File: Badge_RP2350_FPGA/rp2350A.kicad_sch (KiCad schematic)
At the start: 33 parts, among them J2 Conn_01x03_Pin, SW1 SW_Push, SW2 SW_Push, U1 RP2350_60QFN, U7 W25Q32JVSS, Y1 ABM8-272-T3

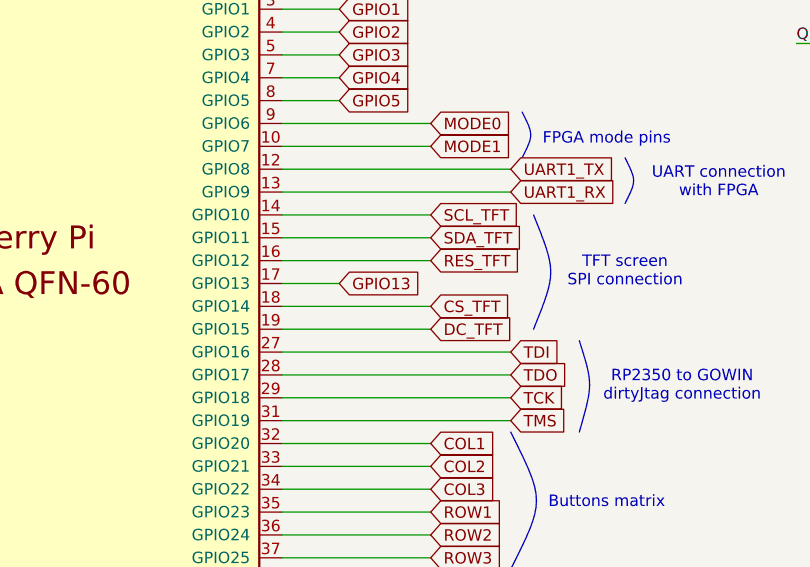
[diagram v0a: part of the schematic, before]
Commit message: add jtagsel_n connection
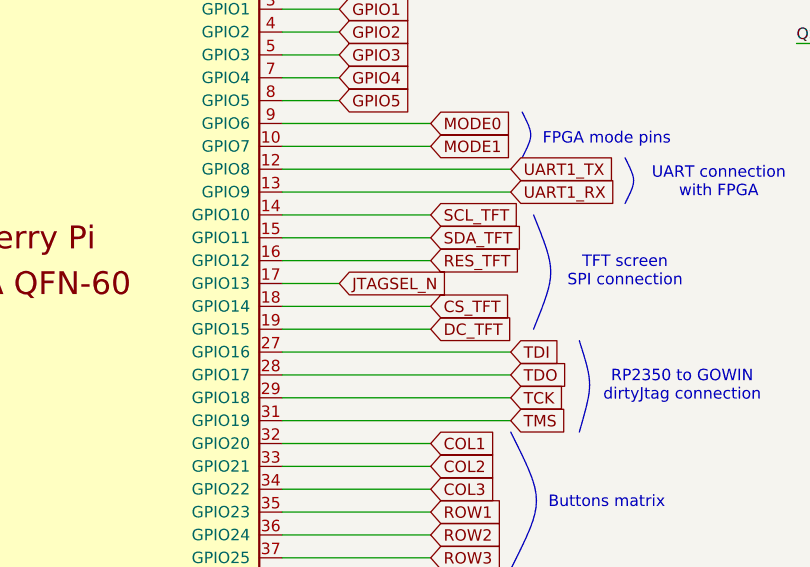
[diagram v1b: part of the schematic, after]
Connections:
- net GPIO13 renamed JTAGSEL_N
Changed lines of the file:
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@@
 		(title "RISC-V Summit Europe Badge")
 		(date "2026-03-29")
-		(rev "v1.4")
+		(rev "v1.42")
 		(company "SemiTO-V, RISC-V Student Team")
 		(comment 3 "License: CERN-OHL-W-2.0")
@@
 		)
 	)
-	(global_label "GPIO13"
-		(shape input)
-		(at 151.13 106.68 0)
-		(fields_autoplaced yes)
-		(effects
-			(font
-				(size 1.27 1.27)
-			)
-			(justify left)
-		)
-		(property "Intersheetrefs" "${INTERSHEET_REFS}"
-			(at 161.0095 106.68 0)
-			(hide yes)
-			(show_name no)
-			(do_not_autoplace no)
-			(effects
-				(font
-					(size 1.27 1.27)
-				)
-				(justify left)
-			)
-		)
-	)
 	(global_label "UART1_RX"
 		(shape input)
@@
 			(hide yes)
 			(show_name no)
+			(do_not_autoplace no)
+			(effects
+				(font
+					(size 1.27 1.27)
+				)
+				(justify left)
+			)
+		)
+	)
+	(global_label "JTAGSEL_N"
+		(shape input)
+		(at 151.13 106.68 0)
+		(fields_autoplaced yes)
+		(effects
+			(font
+				(size 1.27 1.27)
+			)
+			(justify left)
+		)
+		(property "Intersheetrefs" "${INTERSHEET_REFS}"
+			(at 164.0937 106.68 0)
+			(hide yes)
+			(show_name no)

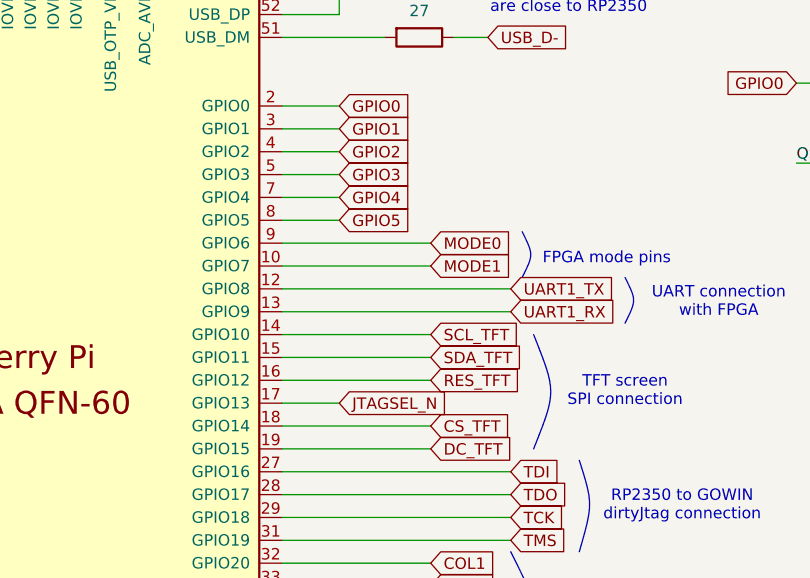
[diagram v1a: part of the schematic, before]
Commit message: add more FPGA connections and generate netlist, bom
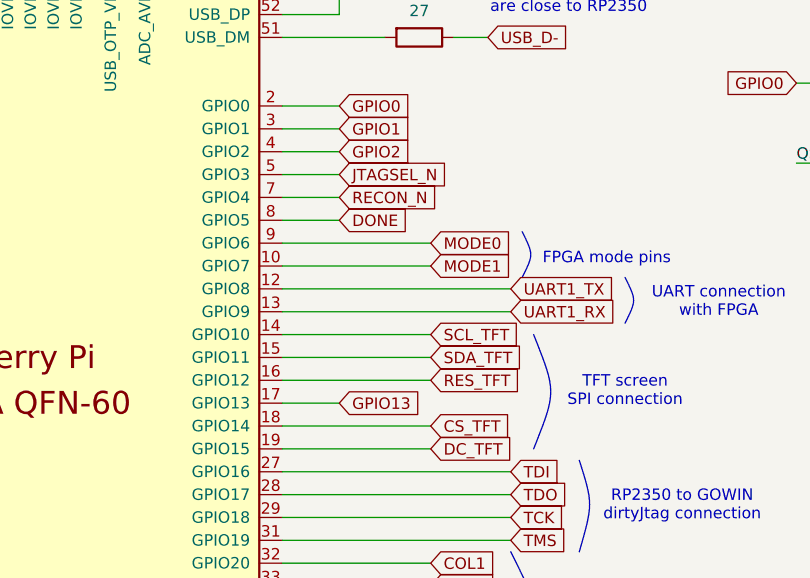
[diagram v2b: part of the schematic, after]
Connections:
- net GPIO3 is gone; now on net JTAGSEL_N: U1.5 (GPIO3)
- net JTAGSEL_N: no longer U1.17 (GPIO13)
- net GPIO4 renamed RECON_N
- net GPIO5 renamed DONE
- new net GPIO13: U1.17 (GPIO13)
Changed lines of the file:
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@@
 		)
 	)
-	(global_label "GPIO3"
+	(global_label "UART1_RX"
+		(shape input)
+		(at 170.18 96.52 0)
+		(fields_autoplaced yes)
+		(effects
+			(font
+				(size 1.27 1.27)
+			)
+			(justify left)
+		)
+		(property "Intersheetrefs" "${INTERSHEET_REFS}"
+			(at 182.4785 96.52 0)
+			(hide yes)
+			(show_name no)
+			(do_not_autoplace no)
+			(effects
+				(font
+					(size 1.27 1.27)
+				)
+				(justify left)
+			)
+		)
+	)
+	(global_label "GPIO28_ADC2"
+		(shape input)
+		(at 151.13 147.32 0)
+		(fields_autoplaced yes)
+		(effects
+			(font
+				(size 1.27 1.27)
+			)
+			(justify left)
+		)
+		(property "Intersheetrefs" "${INTERSHEET_REFS}"
+			(at 166.8152 147.32 0)
+			(hide yes)
+			(show_name no)
+			(do_not_autoplace no)
+			(effects
+				(font
+					(size 1.27 1.27)
+				)
+				(justify left)
+			)
+		)
+	)
+	(global_label "GPIO27_ADC1"
+		(shape input)
+		(at 151.13 144.78 0)
+		(fields_autoplaced yes)
+		(effects
+			(font
+				(size 1.27 1.27)
+			)
+			(justify left)
+		)
+		(property "Intersheetrefs" "${INTERSHEET_REFS}"
+			(at 166.8152 144.78 0)
+			(hide yes)
+			(show_name no)
+			(do_not_autoplace no)
+			(effects
+				(font
+					(size 1.27 1.27)
+				)
+				(justify left)
+			)
+		)
+	)
+	(global_label "JTAGSEL_N"
 		(shape input)
 		(at 151.13 81.28 0)
@@
 		)
 		(property "Intersheetrefs" "${INTERSHEET_REFS}"
-			(at 159.8 81.28 0)
-			(hide yes)
-			(show_name no)
-			(do_not_autoplace no)
-			(effects
-				(font
-					(size 1.27 1.27)
-				)
-				(justify left)
-			)
-		)
-	)
-	(global_label "UART1_RX"
-		(shape input)
-		(at 170.18 96.52 0)
-		(fields_autoplaced yes)
-		(effects
-			(font
-				(size 1.27 1.27)
-			)
-			(justify left)
-		)
-		(property "Intersheetrefs" "${INTERSHEET_REFS}"
-			(at 182.4785 96.52 0)
-			(hide yes)
-			(show_name no)
-			(do_not_autoplace no)
-			(effects
-				(font
-					(size 1.27 1.27)
-				)
-				(justify left)
-			)
-		)
-	)
-	(global_label "GPIO28_ADC2"
-		(shape input)
-		(at 151.13 147.32 0)
-		(fields_autoplaced yes)
-		(effects
-			(font
-				(size 1.27 1.27)
-			)
-			(justify left)
-		)
-		(property "Intersheetrefs" "${INTERSHEET_REFS}"
-			(at 166.8152 147.32 0)
-			(hide yes)
-			(show_name no)
-			(do_not_autoplace no)
-			(effects
-				(font
-					(size 1.27 1.27)
-				)
-				(justify left)
-			)
-		)
-	)
-	(global_label "GPIO27_ADC1"
-		(shape input)
-		(at 151.13 144.78 0)
-		(fields_autoplaced yes)
-		(effects
-			(font
-				(size 1.27 1.27)
-			)
-			(justify left)
-		)
-		(property "Intersheetrefs" "${INTERSHEET_REFS}"
-			(at 166.8152 144.78 0)
+			(at 164.0937 81.28 0)
 			(hide yes)
 			(show_name no)
@@
 		)
 	)
+	(global_label "DONE"
+		(shape input)
+		(at 151.13 86.36 0)
+		(fields_autoplaced yes)
+		(effects
+			(font
+				(size 1.27 1.27)
+			)
+			(justify left)
+		)
+		(property "Intersheetrefs" "${INTERSHEET_REFS}"
+			(at 159.1952 86.36 0)
+			(hide yes)
+			(show_name no)
+			(do_not_autoplace no)
+			(effects
+				(font
+					(size 1.27 1.27)
+				)
+				(justify left)
+			)
+		)
+	)
 	(global_label "SDA_TFT"
 		(shape input)
@@
 		)
 	)
+	(global_label "RECON_N"
+		(shape input)
+		(at 151.13 83.82 0)
+		(fields_autoplaced yes)
+		(effects
+			(font
+				(size 1.27 1.27)
+			)
+			(justify left)
+		)
+		(property "Intersheetrefs" "${INTERSHEET_REFS}"
+			(at 162.7633 83.82 0)
+			(hide yes)
+			(show_name no)
+			(do_not_autoplace no)
+			(effects
+				(font
+					(size 1.27 1.27)
+				)
+				(justify left)
+			)
+		)
+	)
+	(global_label "GPIO13"
+		(shape input)
+		(at 151.13 106.68 0)
+		(fields_autoplaced yes)
+		(effects
+			(font
+				(size 1.27 1.27)
+			)
+			(justify left)
+		)
+		(property "Intersheetrefs" "${INTERSHEET_REFS}"
+			(at 161.0095 106.68 0)
+			(hide yes)
+			(show_name no)
+			(do_not_autoplace no)
+			(effects
+				(font
+					(size 1.27 1.27)
+				)
+				(justify left)
+			)
+		)
+	)
 	(global_label "GPIO29_ADC3"
 		(shape input)
@@
 		)
 	)
-	(global_label "GPIO5"
-		(shape input)
-		(at 151.13 86.36 0)
-		(fields_autoplaced yes)
-		(effects
-			(font
-				(size 1.27 1.27)
-			)
-			(justify left)
-		)
-		(property "Intersheetrefs" "${INTERSHEET_REFS}"
-			(at 159.8 86.36 0)
-			(hide yes)
-			(show_name no)
-			(do_not_autoplace no)
-			(effects
-				(font
-					(size 1.27 1.27)
-				)
-				(justify left)
-			)
-		)
-	)
-	(global_label "JTAGSEL_N"
-		(shape input)
-		(at 151.13 106.68 0)
-		(fields_autoplaced yes)
-		(effects
-			(font
-				(size 1.27 1.27)
-			)
-			(justify left)
-		)
-		(property "Intersheetrefs" "${INTERSHEET_REFS}"
-			(at 164.0937 106.68 0)
-			(hide yes)
-			(show_name no)
-			(do_not_autoplace no)
-			(effects
-				(font
-					(size 1.27 1.27)
-				)
-				(justify left)
-			)
-		)
-	)
 	(global_label "COL2"
 		(shape input)
@@
 			(hide yes)
 			(show_name no)
-			(do_not_autoplace no)
-			(effects
-				(font
-					(size 1.27 1.27)
-				)
-				(justify left)
-			)
-		)
-	)
-	(global_label "GPIO4"
-		(shape input)
-		(at 151.13 83.82 0)
-		(fields_autoplaced yes)
-		(effects
-			(font
-				(size 1.27 1.27)
-			)
-			(justify left)
-		)
-		(property "Intersheetrefs" "${INTERSHEET_REFS}"
-			(at 159.8 83.82 0)
-			(hide yes)
-			(show_name no)

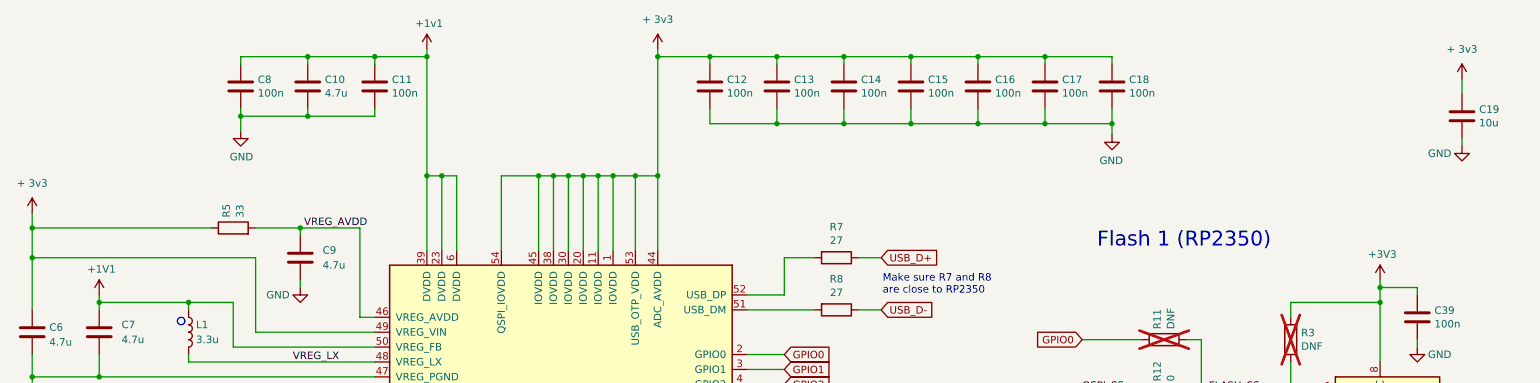
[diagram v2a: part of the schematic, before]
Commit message: update footprints, connections, some labels and more
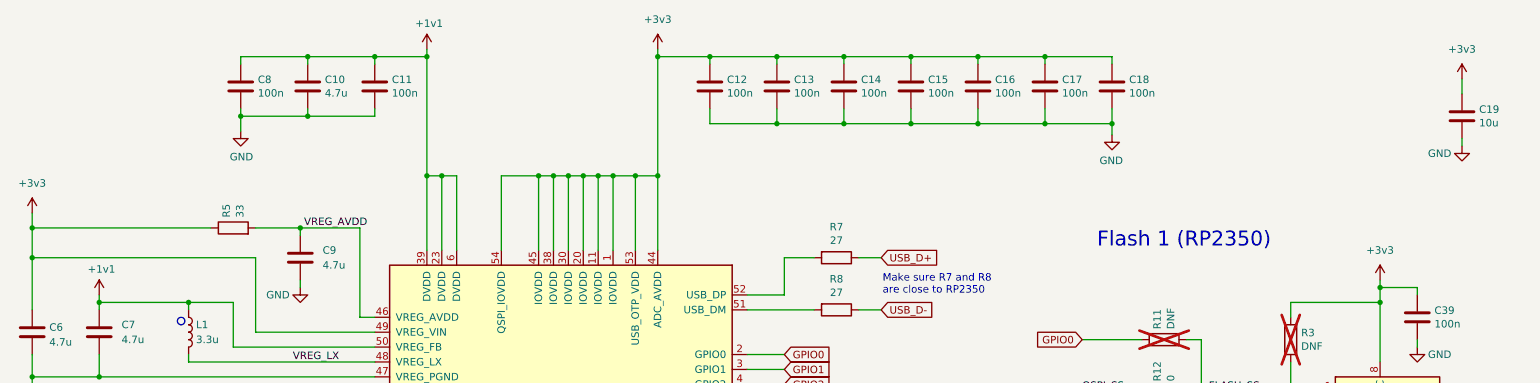
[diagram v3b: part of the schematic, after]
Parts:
- SW1, SW2: footprint Button_Switch_SMD:SW_SPST_B3U-1000P -> semitovpartslibrary:C&K KMR621NGLFS
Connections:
- net +1V1 is gone; now on net +1v1: C7.1, L1.1, U1.50 (VREG_FB)
- net +3V3 is gone; now on net +3v3: C39.1, R3.1, U7.8 (VCC)
- net + 3v3 renamed +3v3

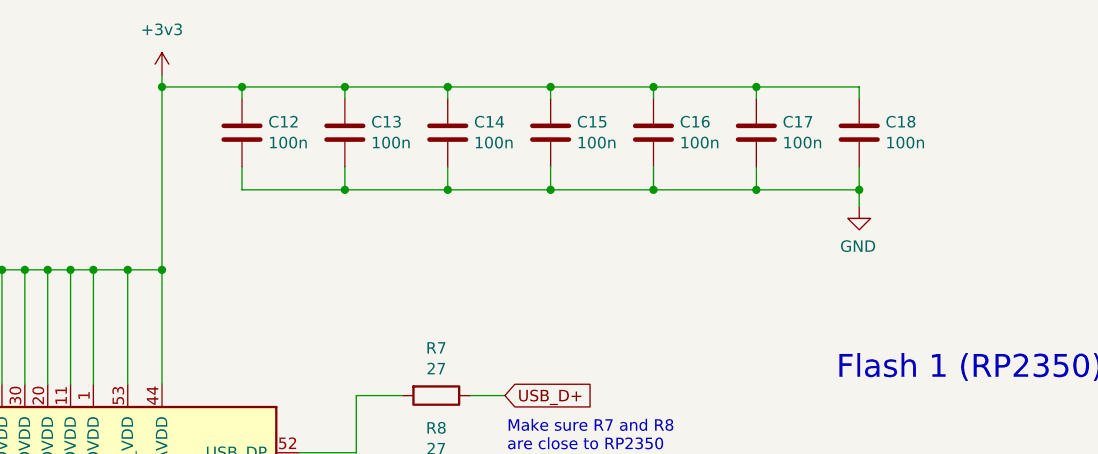
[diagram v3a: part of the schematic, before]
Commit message: M: pcb routing start, minor schematic changes
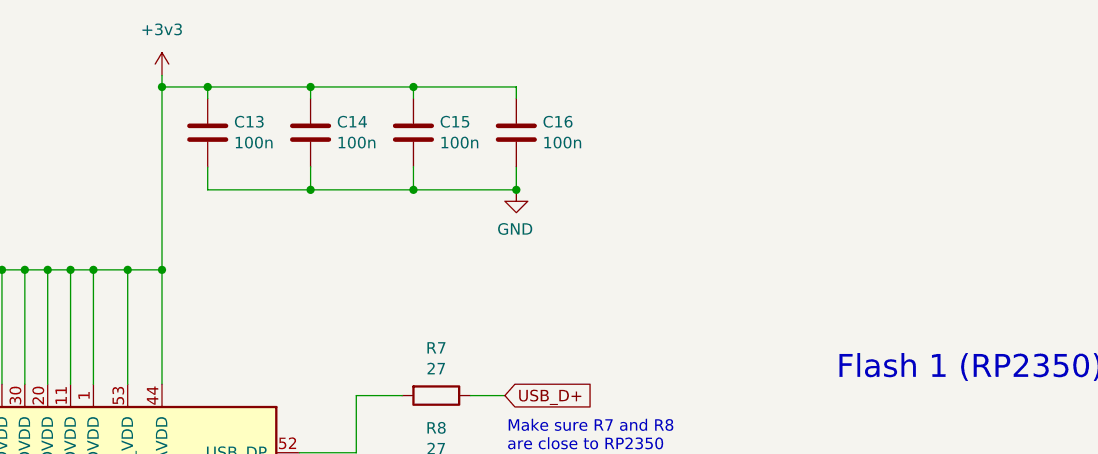
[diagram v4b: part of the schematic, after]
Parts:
- removed C12, C17, C18: 100n, Capacitor_SMD:C_0402_1005Metric, symbol Device:C
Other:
- moved on the sheet: C13, C14, C15, C16

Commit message: finalize the design, add photos
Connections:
- net MODE0: no longer names the net of U1.9 (GPIO6)
- net MODE1: no longer names the net of U1.10 (GPIO7)
- no-connect marks 0 -> 2
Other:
- note removed: "FPGA mode pins"
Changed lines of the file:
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@@
 		(title "RISC-V Summit Europe Badge")
 		(date "2026-03-29")
-		(rev "v1.5")
+		(rev "v1.52")
 		(company "SemiTO-V, RISC-V Student Team")
 		(comment 3 "License: CERN-OHL-W-2.0")
@@
 		)
 	)
-	(bezier
-		(pts
-			(xy 171.45 87.63) (xy 172.72 90.17) (xy 172.72 90.17) (xy 171.45 92.71)
-		)
-		(stroke
-			(width 0)
-			(type default)
-		)
-		(fill
-			(type none)
-		)
-	)
 	(circle
 		(center 48.26 67.945)
@@
 		)
 	)
-	(text "FPGA mode pins"
-		(exclude_from_sim no)
-		(at 180.848 90.678 0)
-		(effects
-			(font
-				(size 1.27 1.27)
-			)
-		)
-	)
 	(text "UART connection\nwith FPGA"
 		(exclude_from_sim no)
@@
 		(color 0 0 0 0)
 	)
+	(no_connect
+		(at 144.78 88.9)
+	)
+	(no_connect
+		(at 144.78 91.44)
+	)
 	(wire
 		(pts
@@
 	(wire
 		(pts
-			(xy 144.78 91.44) (xy 161.29 91.44)
-		)
-		(stroke
-			(width 0)
-			(type default)
-		)
-	)
-	(wire
-		(pts
 			(xy 81.28 85.09) (xy 62.865 85.09)
 		)
@@
 		(pts
 			(xy 69.85 22.86) (xy 81.28 22.86)
-		)
-		(stroke
-			(width 0)
-			(type default)
-		)
-	)
-	(wire
-		(pts
-			(xy 144.78 88.9) (xy 161.29 88.9)
 		)
 		(stroke
@@
 		)
 	)
-	(global_label "MODE1"
-		(shape input)
-		(at 161.29 91.44 0)
+	(global_label "COL3"
+		(shape input)
+		(at 161.29 129.54 0)
 		(fields_autoplaced yes)
 		(effects
@@
 		)
 		(property "Intersheetrefs" "${INTERSHEET_REFS}"
-			(at 170.6856 91.44 0)
+			(at 169.1133 129.54 0)
 			(hide yes)
 			(show_name no)
@@
 		)
 	)
-	(global_label "COL3"
-		(shape input)
-		(at 161.29 129.54 0)
+	(global_label "SCL_TFT"
+		(shape input)
+		(at 161.29 99.06 0)
 		(fields_autoplaced yes)
 		(effects
@@
 		)
 		(property "Intersheetrefs" "${INTERSHEET_REFS}"
-			(at 169.1133 129.54 0)
+			(at 171.7742 99.06 0)
 			(hide yes)
 			(show_name no)
@@
 		)
 	)
-	(global_label "SCL_TFT"
-		(shape input)
-		(at 161.29 99.06 0)
+	(global_label "CS_TFT"
+		(shape input)
+		(at 161.29 109.22 0)
 		(fields_autoplaced yes)
 		(effects
@@
 		)
 		(property "Intersheetrefs" "${INTERSHEET_REFS}"
-			(at 171.7742 99.06 0)
-			(hide yes)
-			(show_name no)
-			(do_not_autoplace no)
-			(effects
-				(font
-					(size 1.27 1.27)
-				)
-				(justify left)
-			)
-		)
-	)
-	(global_label "CS_TFT"
-		(shape input)
-		(at 161.29 109.22 0)
-		(fields_autoplaced yes)
-		(effects
-			(font
-				(size 1.27 1.27)
-			)
-			(justify left)
-		)
-		(property "Intersheetrefs" "${INTERSHEET_REFS}"
 			(at 170.7461 109.22 0)
 			(hide yes)
 			(show_name no)
-			(do_not_autoplace no)
-			(effects
-				(font
-					(size 1.27 1.27)
-				)
-				(justify left)
-			)
-		)
-	)
-	(global_label "MODE0"
-		(shape input)
-		(at 161.29 88.9 0)
-		(fields_autoplaced yes)
-		(effects
-			(font
-				(size 1.27 1.27)
-			)
-			(justify left)
-		)
-		(property "Intersheetrefs" "${INTERSHEET_REFS}"
-			(at 170.6856 88.9 0)
-			(hide yes)
-			(show_name no)
